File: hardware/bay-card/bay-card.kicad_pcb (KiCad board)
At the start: 4 copper layers, 45 x 37.6 mm, 39 parts, among them J1 bay card edge, J2 SATA 22-pin, Q1 AON7403, Q2 AON7403, Q3 2N7002, Q4 2N7002, U1 ASM1153E, Y1 30MHz CL=16pF

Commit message: docs+hw: re-render all boards, electronics, case and full unit; engineer hand-off guide, review pack, generated BOM, renders doc; lint cleanup
Co-Authored-By: Claude Sonnet 5 <noreply@anthropic.com>
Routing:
- net USB2_DM: vias 3 -> 2
- net U1_XI: vias 4 -> 3
- net U1_VCCO: vias 9 -> 8
- net 5V_BAY_SW: vias 5 -> 2
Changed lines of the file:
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@@
 	)
 	(via
-		(at 44.075 52.025)
-		(size 0.3)
-		(drill 0.15)
-		(layers "F.Cu" "B.Cu")
-		(net 5)
-	)
-	(via
-		(at 43.475 53.325)
-		(size 0.3)
-		(drill 0.15)
-		(layers "F.Cu" "B.Cu")
-		(net 5)
-	)
-	(via
 		(at 30.1028 51.9412)
 		(size 0.6)
@@
 		(net 5)
 	)
-	(via
-		(at 43.475 52.675)
-		(size 0.3)
-		(drill 0.15)
-		(layers "F.Cu" "B.Cu")
-		(net 5)
-	)
 	(segment
 		(start 43.475 51.375)
@@
 		(net 28)
 	)
-	(via
-		(at 61.675 41.5)
-		(size 0.3)
-		(drill 0.15)
-		(layers "F.Cu" "B.Cu")
-		(net 28)
-	)
 	(segment
 		(start 59.8 36.825)
@@
 	)
 	(via
-		(at 54.325 38.3)
-		(size 0.3)
-		(drill 0.15)
-		(layers "F.Cu" "B.Cu")
-		(net 30)
-	)
-	(via
 		(at 51.2002 46.03)
 		(size 0.45)
@@
 		(net 32)
 	)
-	(via
-		(at 39.6965 57.7141)
-		(size 0.45)
-		(drill 0.2)
-		(layers "F.Cu" "B.Cu")
-		(net 32)
-	)

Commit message: enclosure+hw: bay-card comb and overhang supports, lid and board branding, fix lid features mirrored front to back
Comb ribs under the lid between receptacle housings, grooved blocks under the card overhang (check_fit.py),
logo and name engraved in the lid, logo/name/URL silkscreen on the brain board, name on the card (branding.py).
Lid windows, OLED, DIP, LEDs and grille were modelled at the wrong end of the lid; corrected and all renders regenerated.

Co-Authored-By: Claude Sonnet 5 <noreply@anthropic.com>
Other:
- board text added: "BRAIN-DRAIN"
- board text added: "bay card"
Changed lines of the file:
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@@
 		(layer "Edge.Cuts")
 	)
+	(gr_text "BRAIN-DRAIN"
+		(at 53.95 58.75 0)
+		(layer "F.SilkS")
+		(effects
+			(font
+				(size 1.174246 1.174246)
+				(thickness 0.3)
+			)
+		)
+	)
+	(gr_text "bay card"
+		(at 53.95 60.674246 0)
+		(layer "F.SilkS")
+		(effects
+			(font
+				(size 1.3 1.3)
+				(thickness 0.18)
+			)
+		)
+	)
 	(gr_text "brain-drain bay card v2  45x46"
 		(at 22 17 0)
@@
 		)
 	)
+	(group "branding"
+		(members "a2e7402b-747e-4434-901d-4ddd77b3a5cc" "aba6498c-c39c-46a9-ad61-7b9e07ddc1f7")
+	)
 	(embedded_fonts no)

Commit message: hw: board revision on the silkscreen and title block; silkscreen renders; lid-plan label fixes
Co-Authored-By: Claude Sonnet 5 <noreply@anthropic.com>
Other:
- board text added: "bay card rev 1.0"
- board text removed: "bay card"
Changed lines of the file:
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@@
 	)
 	(paper "A3")
+	(title_block
+		(rev "1.0")
+	)
 	(layers
 		(0 "F.Cu" signal)
@@
 		(layer "Edge.Cuts")
 	)
-	(gr_text "BRAIN-DRAIN"
-		(at 53.95 58.75 0)
+	(gr_text "bay card rev 1.0"
+		(at 53.95 60.674246 0)
 		(layer "F.SilkS")
 		(effects
 			(font
-				(size 1.174246 1.174246)
-				(thickness 0.3)
+				(size 0.954075 0.954075)
+				(thickness 0.18)
 			)
 		)
 	)
-	(gr_text "bay card"
-		(at 53.95 60.674246 0)
+	(gr_text "BRAIN-DRAIN"
+		(at 53.95 58.75 0)
 		(layer "F.SilkS")
 		(effects
 			(font
-				(size 1.3 1.3)
-				(thickness 0.18)
+				(size 1.174246 1.174246)
+				(thickness 0.3)
 			)
 		)
@@
 	)
 	(group "branding"
-		(members "a2e7402b-747e-4434-901d-4ddd77b3a5cc" "aba6498c-c39c-46a9-ad61-7b9e07ddc1f7")
+		(members "8a0da36d-5130-4e9d-b600-eb76e5f37466" "9311a253-9769-4960-8c1c-6356ccb31694")
 	)
 	(embedded_fonts no)

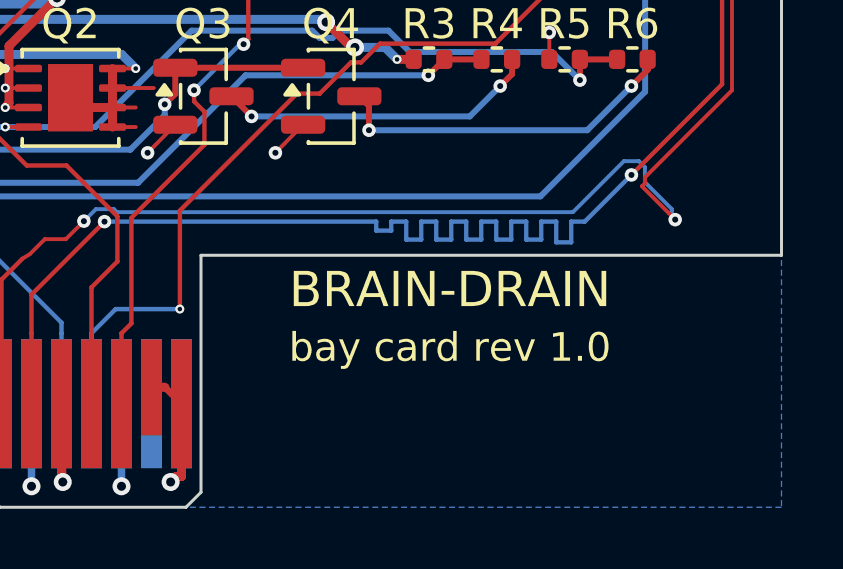
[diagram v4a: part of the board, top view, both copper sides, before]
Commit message: hw: simplified, larger silkscreen logo; eight-bay wording; card label
Co-Authored-By: Claude Sonnet 5 <noreply@anthropic.com>
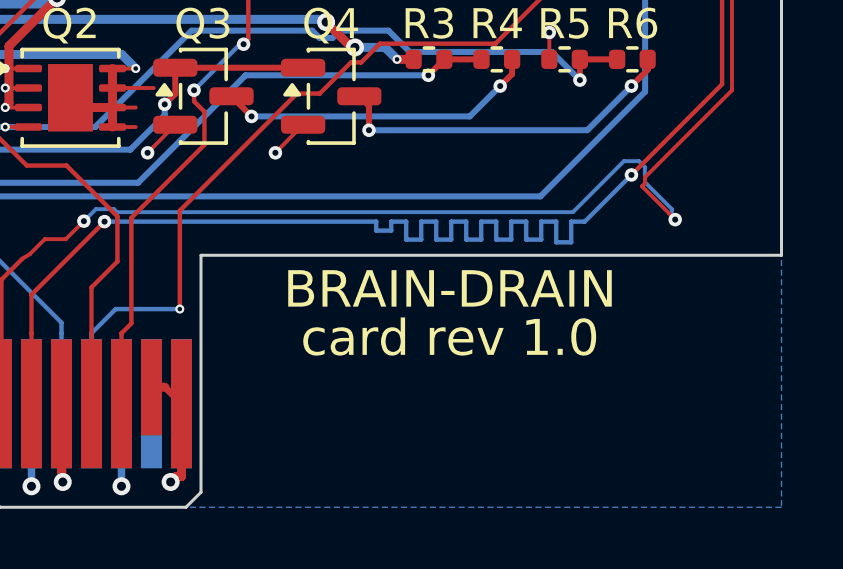
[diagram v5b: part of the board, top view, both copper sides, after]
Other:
- board text added: "card rev 1.0"
- board text removed: "bay card rev 1.0"
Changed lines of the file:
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@@
 		(layer "Edge.Cuts")
 	)
-	(gr_text "bay card rev 1.0"
-		(at 53.95 60.674246 0)
+	(gr_text "card rev 1.0"
+		(at 53.95 60.36637 0)
 		(layer "F.SilkS")
 		(effects
 			(font
-				(size 0.954075 0.954075)
+				(size 1.2 1.2)
 				(thickness 0.18)
 			)
@@
 		(effects
 			(font
-				(size 1.174246 1.174246)
+				(size 1.21637 1.21637)
 				(thickness 0.3)
 			)
@@
 	)
 	(group "branding"
-		(members "8a0da36d-5130-4e9d-b600-eb76e5f37466" "9311a253-9769-4960-8c1c-6356ccb31694")
+		(members "b63345a0-cbae-4ff2-9fdc-07bbd9892c13" "ffa0bc46-6e79-43e9-8d24-0a3e05dddc2f")
 	)
 	(embedded_fonts no)
